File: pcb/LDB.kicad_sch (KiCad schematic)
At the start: 79 parts, among them J1 Conn_01x10_Socket, J10 Conn_01x04_Socket, J11 Conn_01x03_Pin, J12 Conn_01x03_Pin, J13 Conn_01x03_Pin, J14 Conn_01x10_Socket, J2 Conn_01x02_Pin, J3 Conn_01x10_Socket, J4 Conn_02x02_Counter_Clockwise, J5 Conn_02x02_Counter_Clockwise, J6 Conn_02x02_Counter_Clockwise, J7 Conn_02x02_Counter_Clockwise, J8 Conn_02x02_Counter_Clockwise, J9 Conn_02x02_Counter_Clockwise, Q1 MMBFJ113, Q10 MMBFJ113, Q11 MMBFJ113, Q12 MMBFJ113, Q13 MMBFJ113, Q14 MMBFJ113, Q15 MMBFJ113, Q16 MMBFJ113, Q17 MMBFJ113, Q2 MMBFJ113, Q3 MMBFJ113, Q4 MMBFJ113, Q5 MMBFJ113, Q6 MMBFJ113, Q7 MMBFJ113, Q8 MMBFJ113, Q9 MMBFJ113, U1 4543

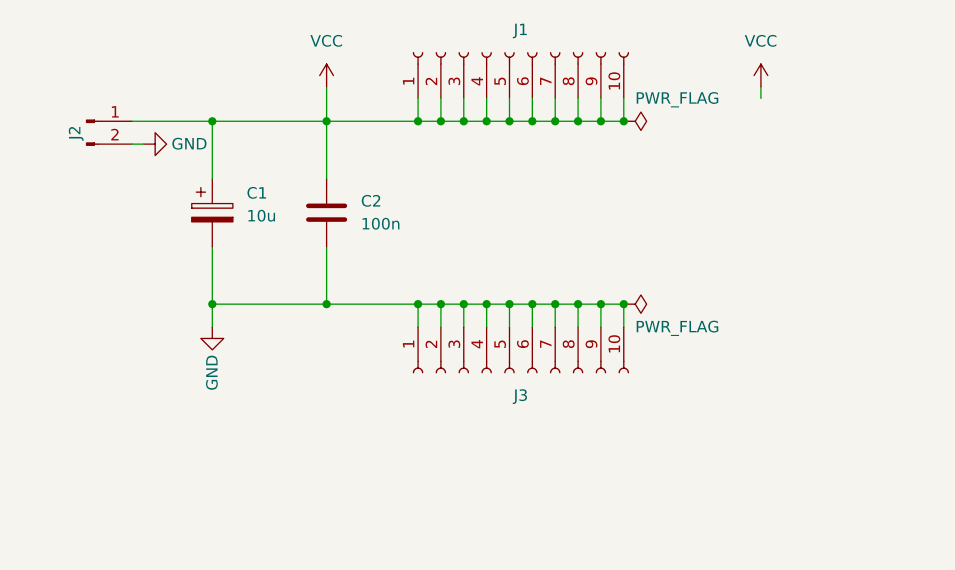
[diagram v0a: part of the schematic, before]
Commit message: Add reverse polarity protection
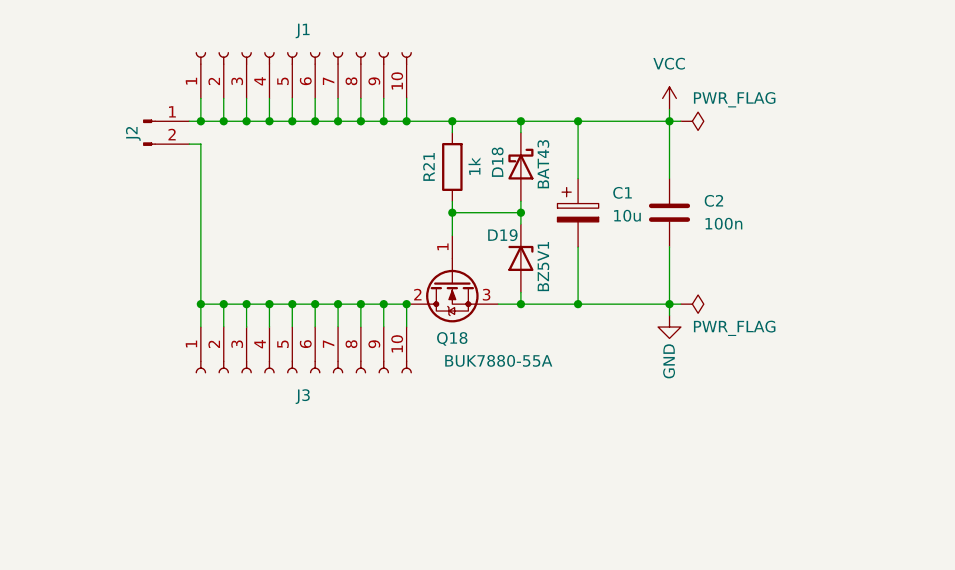
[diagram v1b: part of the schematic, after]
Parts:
- added D18: BAT43, Diode_SMD:D_MiniMELF, symbol Device:D_Schottky
- added D19: BZ5V1, Diode_SMD:D_MiniMELF, symbol Diode:BZV55B15
- added Q18: BUK7880-55A, Package_TO_SOT_SMD:SOT-223-3_TabPin2, symbol Transistor_FET:BUK7880-55A
- added R21: 1k, Resistor_SMD:R_1206_3216Metric, symbol Device:R
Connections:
- net GND: now also D19.2 (A), Q18.3 (S); no longer J2.2 (Pin_2), J3.1 (Pin_1), J3.10 (Pin_10), J3.2 (Pin_2), J3.3 (Pin_3), J3.4 (Pin_4), J3.5 (Pin_5), J3.6 (Pin_6), J3.7 (Pin_7), J3.8 (Pin_8), J3.9 (Pin_9)
- net VCC: now also D18.1 (K), R21.2
- new net: D18.2 (A), D19.1 (K), Q18.1 (G), R21.1
- new net: J2.2 (Pin_2), J3.1 (Pin_1), J3.10 (Pin_10), J3.2 (Pin_2), J3.3 (Pin_3), J3.4 (Pin_4), J3.5 (Pin_5), J3.6 (Pin_6), J3.7 (Pin_7), J3.8 (Pin_8), J3.9 (Pin_9), Q18.2 (D)
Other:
- moved on the sheet: C1, C2, J1, J2, J3
